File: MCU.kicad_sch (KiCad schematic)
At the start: 21 parts, among them U3 M95256-WMN6P, U4 STM32G474RETx, U5 TCAN1044V-Q1

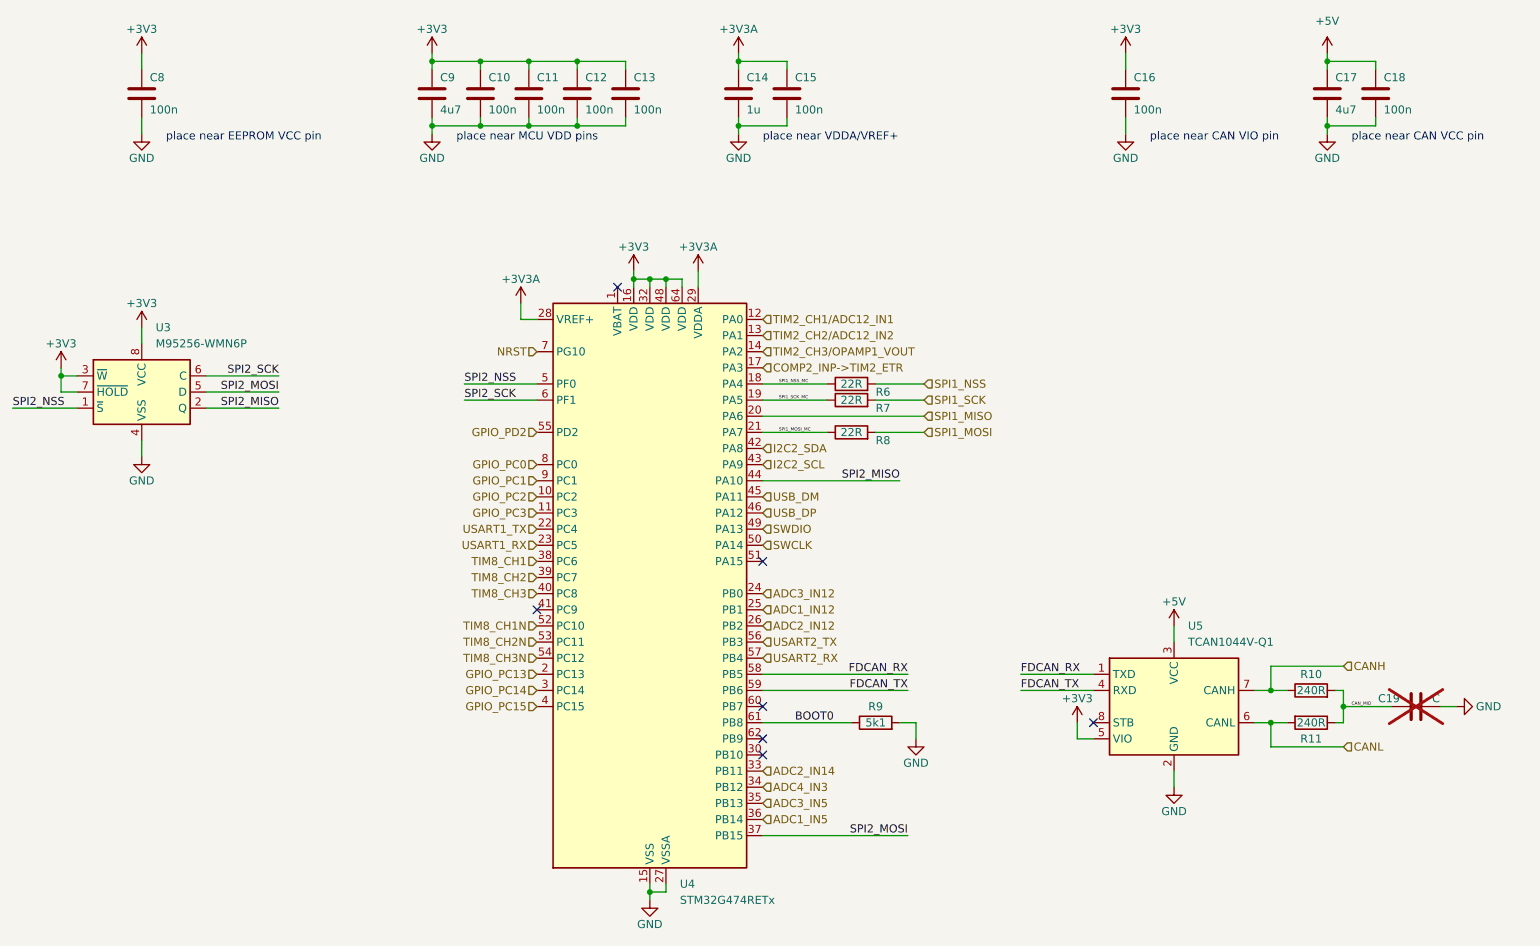
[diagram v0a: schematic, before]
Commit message: Updated schematic to use HRTIM1 and reviewed
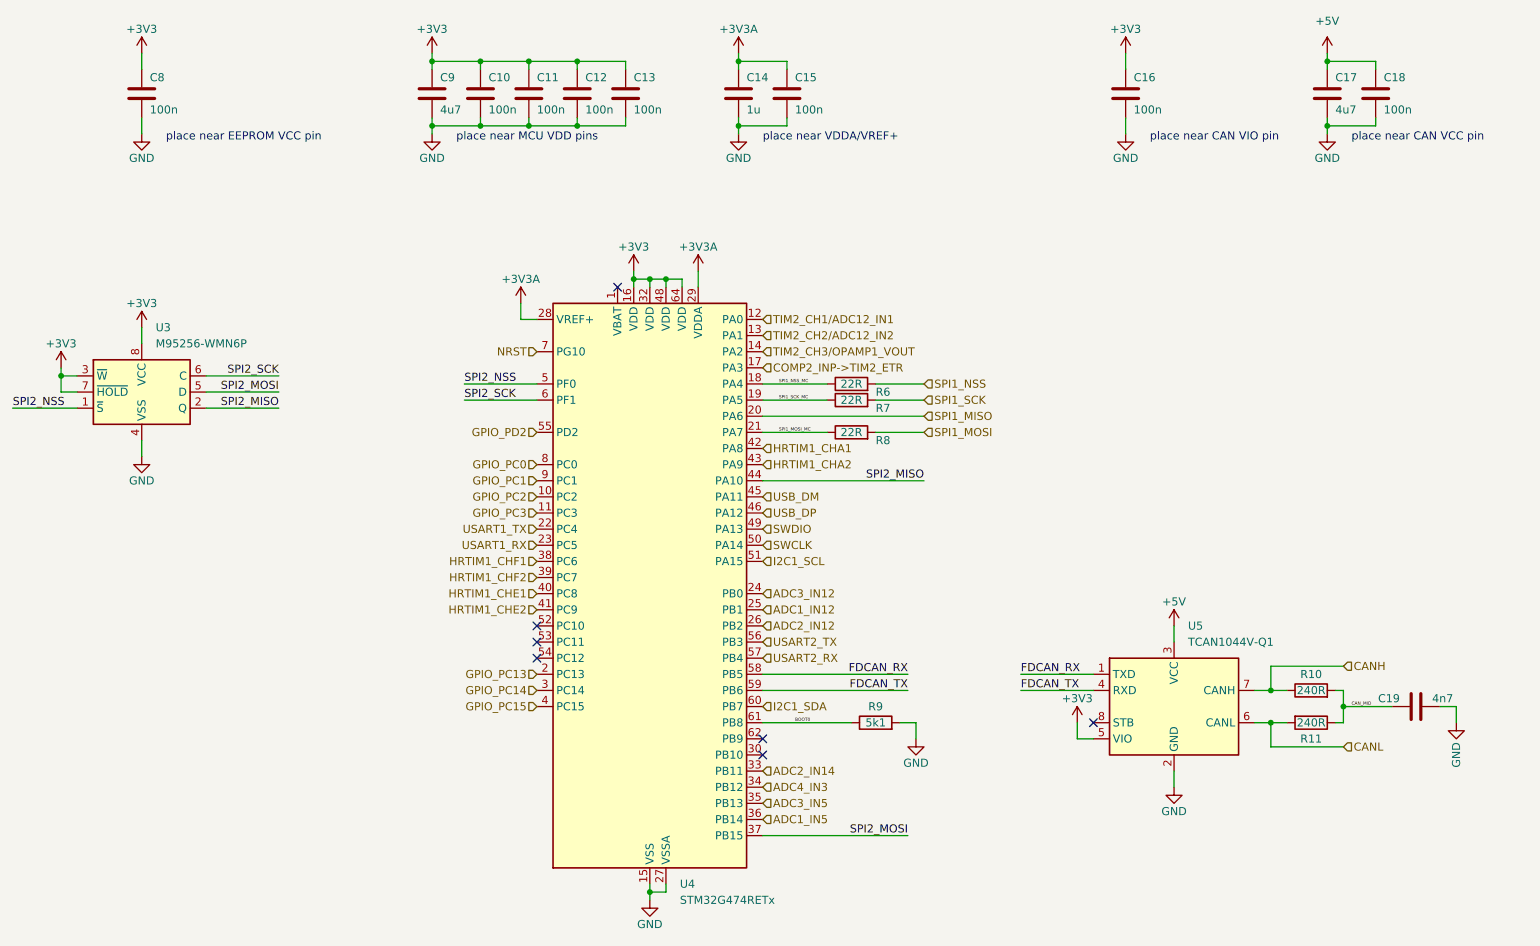
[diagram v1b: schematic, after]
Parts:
- C19: value C -> 4n7; now fitted
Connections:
- net HRTIM1_CHE2: now reaches U4.41 (PC9)
- net I2C1_SCL: now reaches U4.51 (PA15)
- net I2C1_SDA: now reaches U4.60 (PB7)
- net I2C2_SCL renamed HRTIM1_CHA2
- net I2C2_SDA renamed HRTIM1_CHA1
- net TIM8_CH1 renamed HRTIM1_CHF1
- net TIM8_CH1N: no longer names the net of U4.52 (PC10)
- net TIM8_CH2 renamed HRTIM1_CHF2
- net TIM8_CH2N: no longer names the net of U4.53 (PC11)
- net TIM8_CH3 renamed HRTIM1_CHE1
- net TIM8_CH3N: no longer names the net of U4.54 (PC12)
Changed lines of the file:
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@@
 	)
 	(no_connect
-		(at 210.82 130.81)
+		(at 123.19 115.57)
 	)
 	(no_connect
-		(at 158.75 133.35)
+		(at 210.82 130.81)
 	)
 	(no_connect
-		(at 123.19 113.03)
+		(at 158.75 133.35)
 	)
 	(no_connect
-		(at 158.75 105.41)
+		(at 123.19 120.65)
 	)
 	(no_connect
-		(at 158.75 128.27)
+		(at 123.19 118.11)
 	)
 	(no_connect
@@
 	(wire
 		(pts
+			(xy 267.97 130.81) (xy 267.97 128.27)
+		)
+		(stroke
+			(width 0)
+			(type default)
+		)
+	)
+	(wire
+		(pts
 			(xy 106.68 35.56) (xy 106.68 36.83)
 		)
@@
 	(wire
 		(pts
-			(xy 158.75 92.71) (xy 180.34 92.71)
+			(xy 158.75 92.71) (xy 184.15 92.71)
 		)
 		(stroke
@@
 	(wire
 		(pts
+			(xy 267.97 128.27) (xy 265.43 128.27)
+		)
+		(stroke
+			(width 0)
+			(type default)
+		)
+	)
+	(wire
+		(pts
 			(xy 180.34 130.81) (xy 182.88 130.81)
 		)
@@
 	(wire
 		(pts
-			(xy 265.43 128.27) (xy 267.97 128.27)
-		)
-		(stroke
-			(width 0)
-			(type default)
-		)
-	)
-	(wire
-		(pts
 			(xy 106.68 26.67) (xy 106.68 25.4)
 		)
@@
 	)
 	(label "SPI2_MISO"
-		(at 180.34 92.71 180)
+		(at 184.15 92.71 180)
 		(effects
 			(font
@@
 		(effects
 			(font
-				(size 1.27 1.27)
+				(size 0.5 0.5)
 			)
 			(justify left bottom)
@@
 		)
 	)
-	(hierarchical_label "TIM8_CH3N"
+	(hierarchical_label "ADC2_IN12"
 		(shape input)
-		(at 123.19 120.65 180)
+		(at 158.75 115.57 0)
 		(effects
 			(font
 				(size 1.27 1.27)
 			)
-			(justify right)
+			(justify left)
 		)
 	)
-	(hierarchical_label "ADC2_IN12"
+	(hierarchical_label "I2C1_SDA"
 		(shape input)
-		(at 158.75 115.57 0)
+		(at 158.75 128.27 0)
 		(effects
 			(font
@@
 		)
 	)
-	(hierarchical_label "TIM8_CH1"
+	(hierarchical_label "HRTIM1_CHF1"
 		(shape input)
 		(at 123.19 105.41 180)
@@
 		)
 	)
-	(hierarchical_label "TIM8_CH1N"
-		(shape input)
-		(at 123.19 115.57 180)
-		(effects
-			(font
-				(size 1.27 1.27)
-			)
-			(justify right)
-		)
-	)
 	(hierarchical_label "SPI1_NSS"
 		(shape input)
@@
 		)
 	)
-	(hierarchical_label "TIM8_CH3"
+	(hierarchical_label "HRTIM1_CHE1"
 		(shape input)
 		(at 123.19 110.49 180)
@@
 		)
 	)
-	(hierarchical_label "I2C2_SDA"
+	(hierarchical_label "HRTIM1_CHA1"
 		(shape input)
 		(at 158.75 87.63 0)
@@
 		)
 	)
+	(hierarchical_label "I2C1_SCL"
+		(shape input)
+		(at 158.75 105.41 0)
+		(effects
+			(font
+				(size 1.27 1.27)
+			)
+			(justify left)
+		)
+	)
 	(hierarchical_label "GPIO_PC1"
 		(shape input)
@@
 		)
 	)
-	(hierarchical_label "I2C2_SCL"
+	(hierarchical_label "HRTIM1_CHE2"
 		(shape input)
-		(at 158.75 90.17 0)
+		(at 123.19 113.03 180)
 		(effects
 			(font
 				(size 1.27 1.27)
 			)
-			(justify left)
+			(justify right)
 		)
 	)
-	(hierarchical_label "SPI1_MISO"
+	(hierarchical_label "HRTIM1_CHA2"
 		(shape input)
-		(at 184.15 82.55 0)
+		(at 158.75 90.17 0)
 		(effects
 			(font
@@
 		)
 	)
-	(hierarchical_label "TIM8_CH2N"
+	(hierarchical_label "SPI1_MISO"
 		(shape input)
-		(at 123.19 118.11 180)
+		(at 184.15 82.55 0)
 		(effects
 			(font
 				(size 1.27 1.27)
 			)
-			(justify right)
+			(justify left)
 		)
 	)
@@
 		)
 	)
-	(hierarchical_label "TIM8_CH2"
+	(hierarchical_label "HRTIM1_CHF2"
 		(shape input)
 		(at 123.19 107.95 180)
@@
 		(in_bom yes)
 		(on_board yes)
-		(dnp yes)
+		(dnp no)
 		(property "Reference" "C19"
 			(at 259.08 127 90)
@@
 			)
 		)
-		(property "Value" "C"
+		(property "Value" "4n7"
 			(at 264.16 127 90)
 			(effects
@@
 	(symbol
 		(lib_id "power:GND")
-		(at 267.97 128.27 90)
+		(at 267.97 130.81 0)
 		(unit 1)
 		(exclude_from_sim no)
@@
 		(dnp no)
 		(property "Reference" "#PWR067"
-			(at 274.32 128.27 0)
+			(at 267.97 137.16 0)
 			(effects
 				(font
@@
 		)
 		(property "Value" "GND"
-			(at 273.05 128.27 90)
+			(at 267.97 135.89 90)
 			(effects
 				(font
@@
 		)
 		(property "Footprint" ""
-			(at 267.97 128.27 0)
+			(at 267.97 130.81 0)
 			(effects
 				(font
@@
 		)
 		(property "Datasheet" ""
-			(at 267.97 128.27 0)
+			(at 267.97 130.81 0)
 			(effects
 				(font
@@
 		)
 		(property "Description" "Power symbol creates a global label with name \"GND\" , ground"
-			(at 267.97 128.27 0)
+			(at 267.97 130.81 0)
 			(effects
 				(font

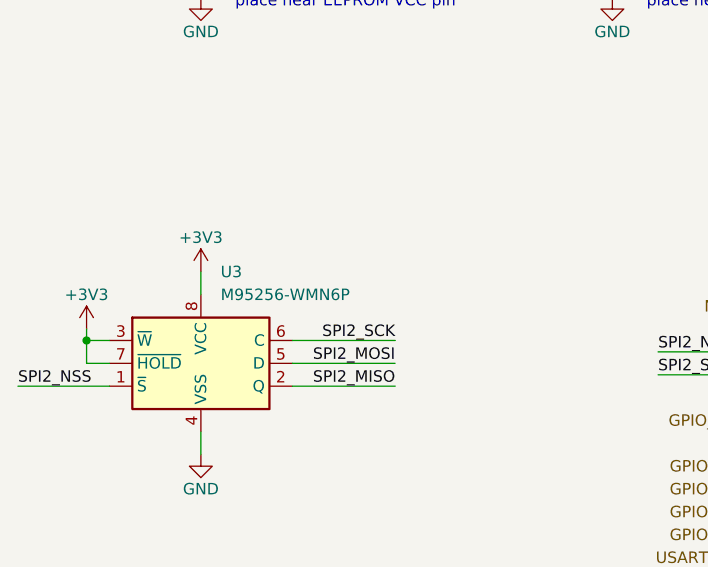
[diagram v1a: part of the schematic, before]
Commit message: Changed EEPROM to TSSOT for smallness
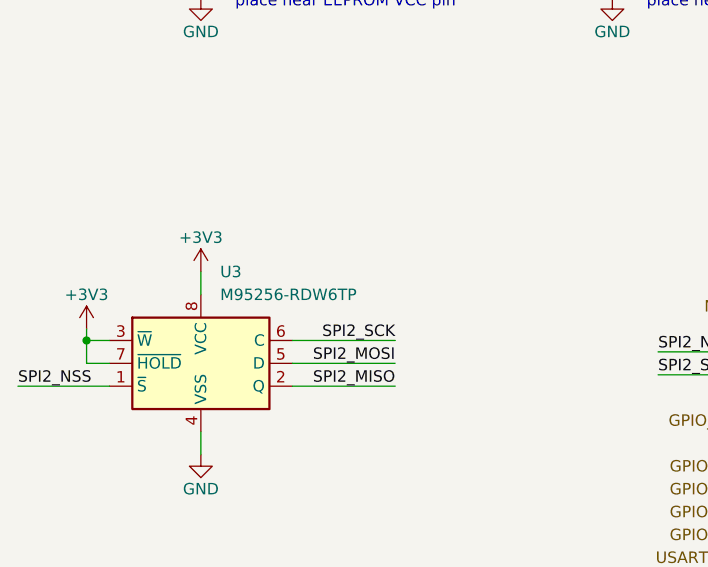
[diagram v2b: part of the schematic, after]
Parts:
- removed U3: M95256-WMN6P, Package_SO:SOIC-8_3.9x4.9mm_P1.27mm, symbol Memory_EEPROM:M95256-WMN6P
- added U3: M95256-RDW6TP, Package_SO:TSSOP-8_4.4x3mm_P0.65mm, symbol User_Memory:M95256-RDW6TP
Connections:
- net +3V3: now also U3.3 (~{W}), U3.7 (~{HOLD}), U3.8 (VCC)
- net GND: now also U3.4 (VSS)
- net SPI2_MISO: now also U3.2 (Q)
- net SPI2_MOSI: now also U3.5 (D)
- net SPI2_NSS: now also U3.1 (~{S})
- net SPI2_SCK: now also U3.6 (C)
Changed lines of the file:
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@@
+	)
+	(symbol
+		(lib_id "User_Memory:M95256-RDW6TP")
+		(at 60.96 78.74 0)
+		(unit 1)
+		(exclude_from_sim no)
+		(in_bom yes)
+		(on_board yes)
+		(dnp no)
+		(fields_autoplaced yes)
+		(property "Reference" "U3"
+			(at 63.1033 68.58 0)
+			(effects
+				(font
+					(size 1.27 1.27)
+				)
+				(justify left)
+			)
+		)
+		(property "Value" "M95256-RDW6TP"
+			(at 63.1033 71.12 0)
+			(effects
+				(font
+					(size 1.27 1.27)
+				)
+				(justify left)
+			)
+		)
+		(property "Footprint" "Package_SO:TSSOP-8_4.4x3mm_P0.65mm"
+			(at 60.96 78.74 0)
+			(effects
+				(font
+					(size 1.27 1.27)
+				)
+				(hide yes)
+			)
+		)
+		(property "Datasheet" "https://www.st.com/content/ccc/resource/technical/document/datasheet/9d/75/f0/3e/76/00/4c/0b/CD00103810.pdf/files/CD00103810.pdf/jcr:content/translations/en.CD00103810.pdf"
+			(at 60.96 78.74 0)
+			(effects
+				(font
+					(size 1.27 1.27)
+				)
+				(hide yes)
+			)
+		)
+		(property "Description" "SPI EEPROM, 256Kb (32K x 8), No Identification Page, 1.8 to 5.5V, TSSOP8"
+			(at 60.96 78.74 0)
+			(effects
+				(font
+					(size 1.27 1.27)
+				)
+				(hide yes)
+			)
+		)
+		(pin "2"
+		)
+		(pin "5"
+		)
+		(pin "6"
+		)
+		(pin "1"
+		)
+		(pin "8"
+		)
+		(pin "4"
+		)
+		(pin "7"
+		)
+		(pin "3"
+		)
+		(instances
+			(project ""
+				(path "/7261d109-8405-40e9-921c-d95f374a7164/92ea675d-7023-4535-8dff-709f4ede5757"
+					(reference "U3")
+					(unit 1)
+				)
+			)
+		)
 	)
 	(symbol
@@
 					(unit 1)
 				)
-			)
-		)
-	)
-	(symbol
-		(lib_id "Memory_EEPROM:M95256-WMN6P")
-		(at 60.96 78.74 0)
-		(unit 1)
-		(exclude_from_sim no)
-		(in_bom yes)
-		(on_board yes)
-		(dnp no)
-		(fields_autoplaced yes)
-		(property "Reference" "U3"
-			(at 63.1541 68.58 0)
-			(effects
-				(font
-					(size 1.27 1.27)
-				)
-				(justify left)
-			)
-		)
-		(property "Value" "M95256-WMN6P"
-			(at 63.1541 71.12 0)
-			(effects
-				(font
-					(size 1.27 1.27)
-				)
-				(justify left)
-			)
-		)
-		(property "Footprint" "Package_SO:SOIC-8_3.9x4.9mm_P1.27mm"
-			(at 60.96 78.74 0)
-			(effects
-				(font
-					(size 1.27 1.27)
-				)
-				(hide yes)
-			)
-		)
-		(property "Datasheet" "http://www.st.com/content/ccc/resource/technical/document/datasheet/9d/75/f0/3e/76/00/4c/0b/CD00103810.pdf/files/CD00103810.pdf/jcr:content/translations/en.CD00103810.pdf"
-			(at 60.96 78.74 0)
-			(effects
-				(font
-					(size 1.27 1.27)
-				)
-				(hide yes)
-			)
-		)
-		(property "Description" "SPI EEPROM, 256Kb (32K x 8), No Identification Page, 2.5 to 5.5V, SO8"
-			(at 60.96 78.74 0)
-			(effects
-				(font
-					(size 1.27 1.27)
-				)
-				(hide yes)
-			)
-		)
-		(pin "2"
-		)
-		(pin "7"
-		)
-		(pin "8"
-		)
-		(pin "1"
-		)
-		(pin "3"
-		)
-		(pin "5"
-		)
-		(pin "6"
-		)
-		(pin "4"
-		)
-		(instances
-			(project "Motor_Control_Brain_Board"
-				(path "/7261d109-8405-40e9-921c-d95f374a7164/92ea675d-7023-4535-8dff-709f4ede5757"
-					(reference "U3")
-					(unit 1)
-				)

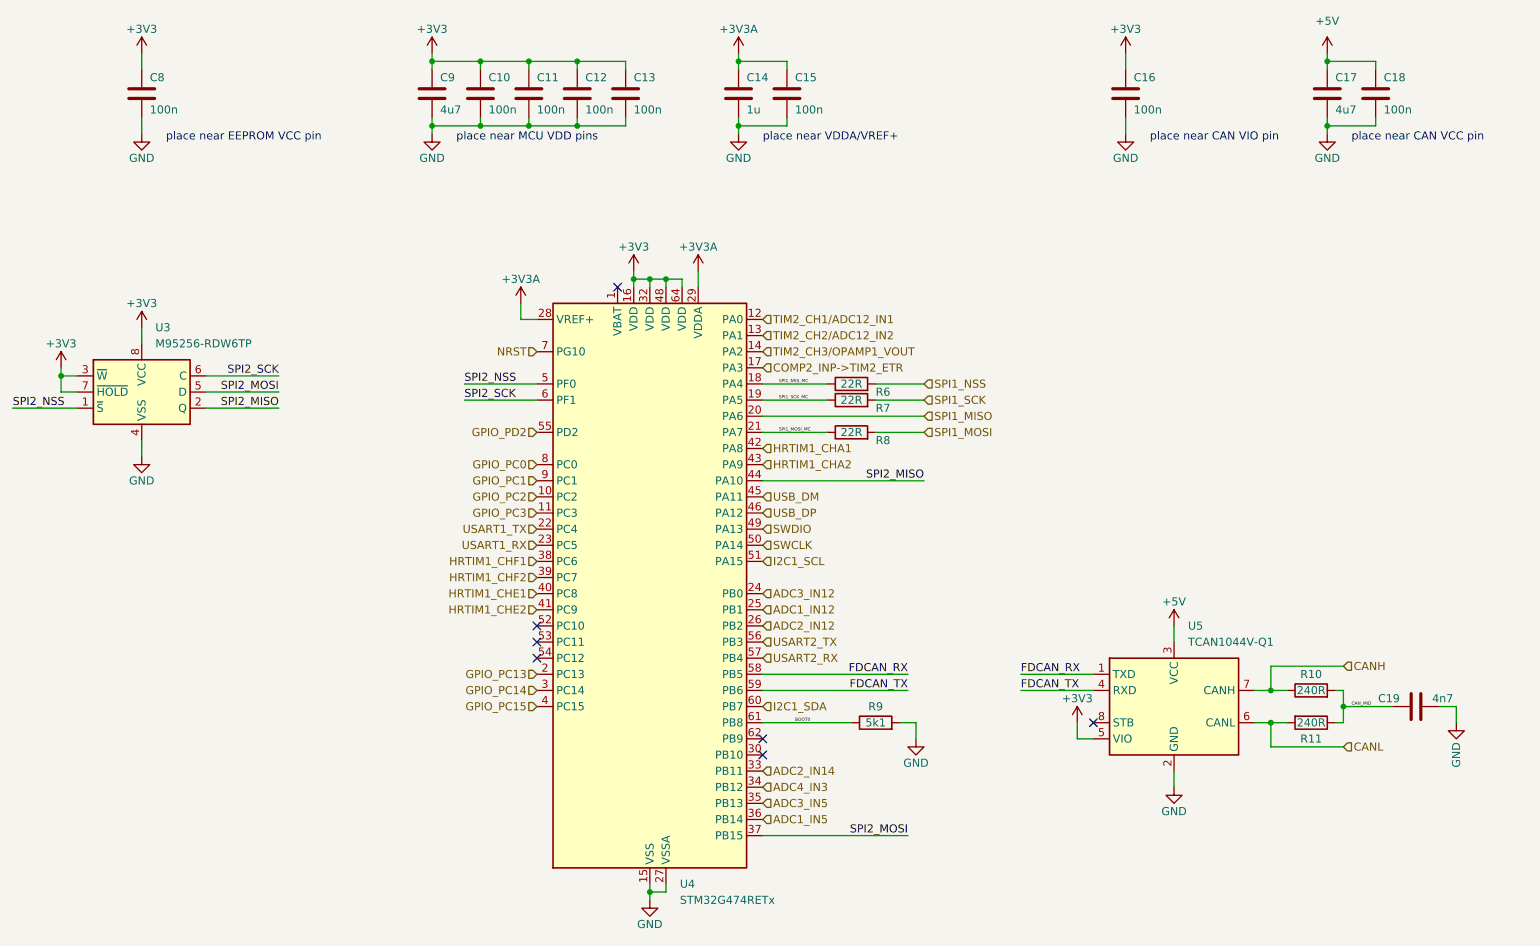
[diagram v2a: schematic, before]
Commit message: Changed to LPUART for 1 channel to improve routing etc. Can now add 1 more ADC as needed. Todo: Figure out GPIO and add oscillator
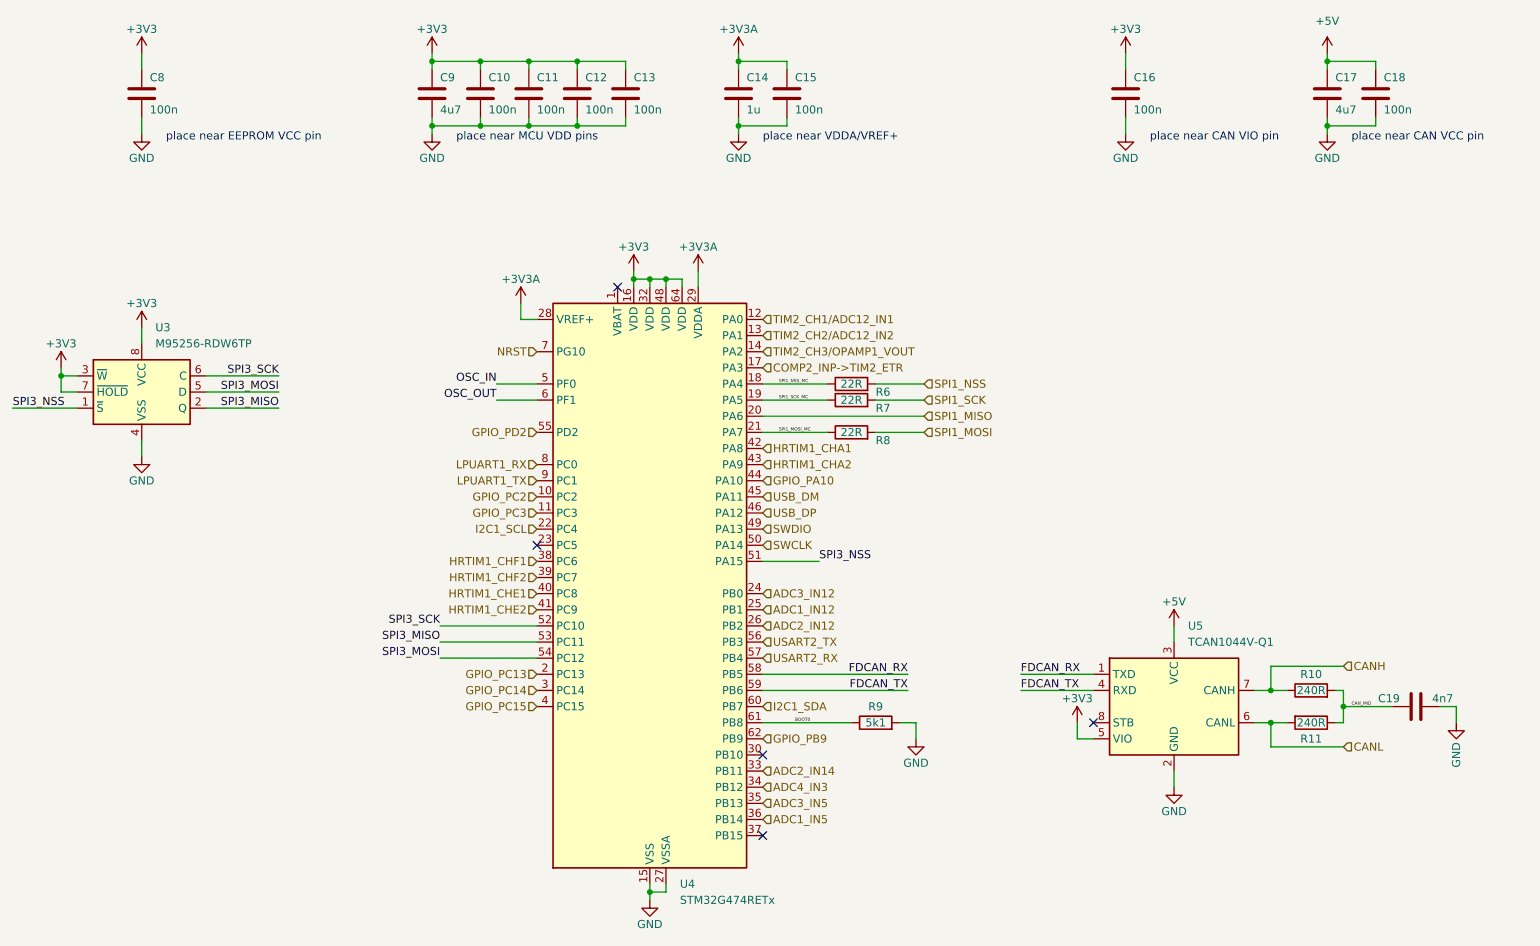
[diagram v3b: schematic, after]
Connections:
- net USART1_TX is gone; now on net I2C1_SCL: U4.22 (PC4)
- net I2C1_SCL: no longer U4.51 (PA15)
- net SPI3_SCK: now reaches U4.52 (PC10)
- net SPI3_SCK: now also U3.6 (C)
- net SPI3_MISO: now reaches U4.53 (PC11)
- net SPI3_MISO: now also U3.2 (Q)
- net SPI3_MOSI: now reaches U4.54 (PC12)
- net SPI3_MOSI: now also U3.5 (D)
- net GPIO_PB9: now reaches U4.62 (PB9)
- net GPIO_PC0 renamed LPUART1_RX
- net GPIO_PC1 renamed LPUART1_TX
- net SPI2_MISO renamed GPIO_PA10
- net GPIO_PA10: no longer U3.2 (Q)
- net SPI2_MOSI: no longer names the net of U4.37 (PB15)
- net SPI2_MOSI: no longer U3.5 (D)
- net SPI2_NSS renamed OSC_IN
- net OSC_IN: no longer U3.1 (~{S})
- net SPI2_SCK renamed OSC_OUT
- net OSC_OUT: no longer U3.6 (C)
- net USART1_RX: no longer names the net of U4.23 (PC5)
- new net SPI3_NSS: U3.1 (~{S}), U4.51 (PA15)
- no-connect marks 7 -> 5
